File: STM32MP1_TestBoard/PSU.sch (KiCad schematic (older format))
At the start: 19 parts, among them Q1 DMG2302U, U3 SE8233X2, U4 TPS54202DDC, U6 STM32G031JxM, U7 MCP603-xCH

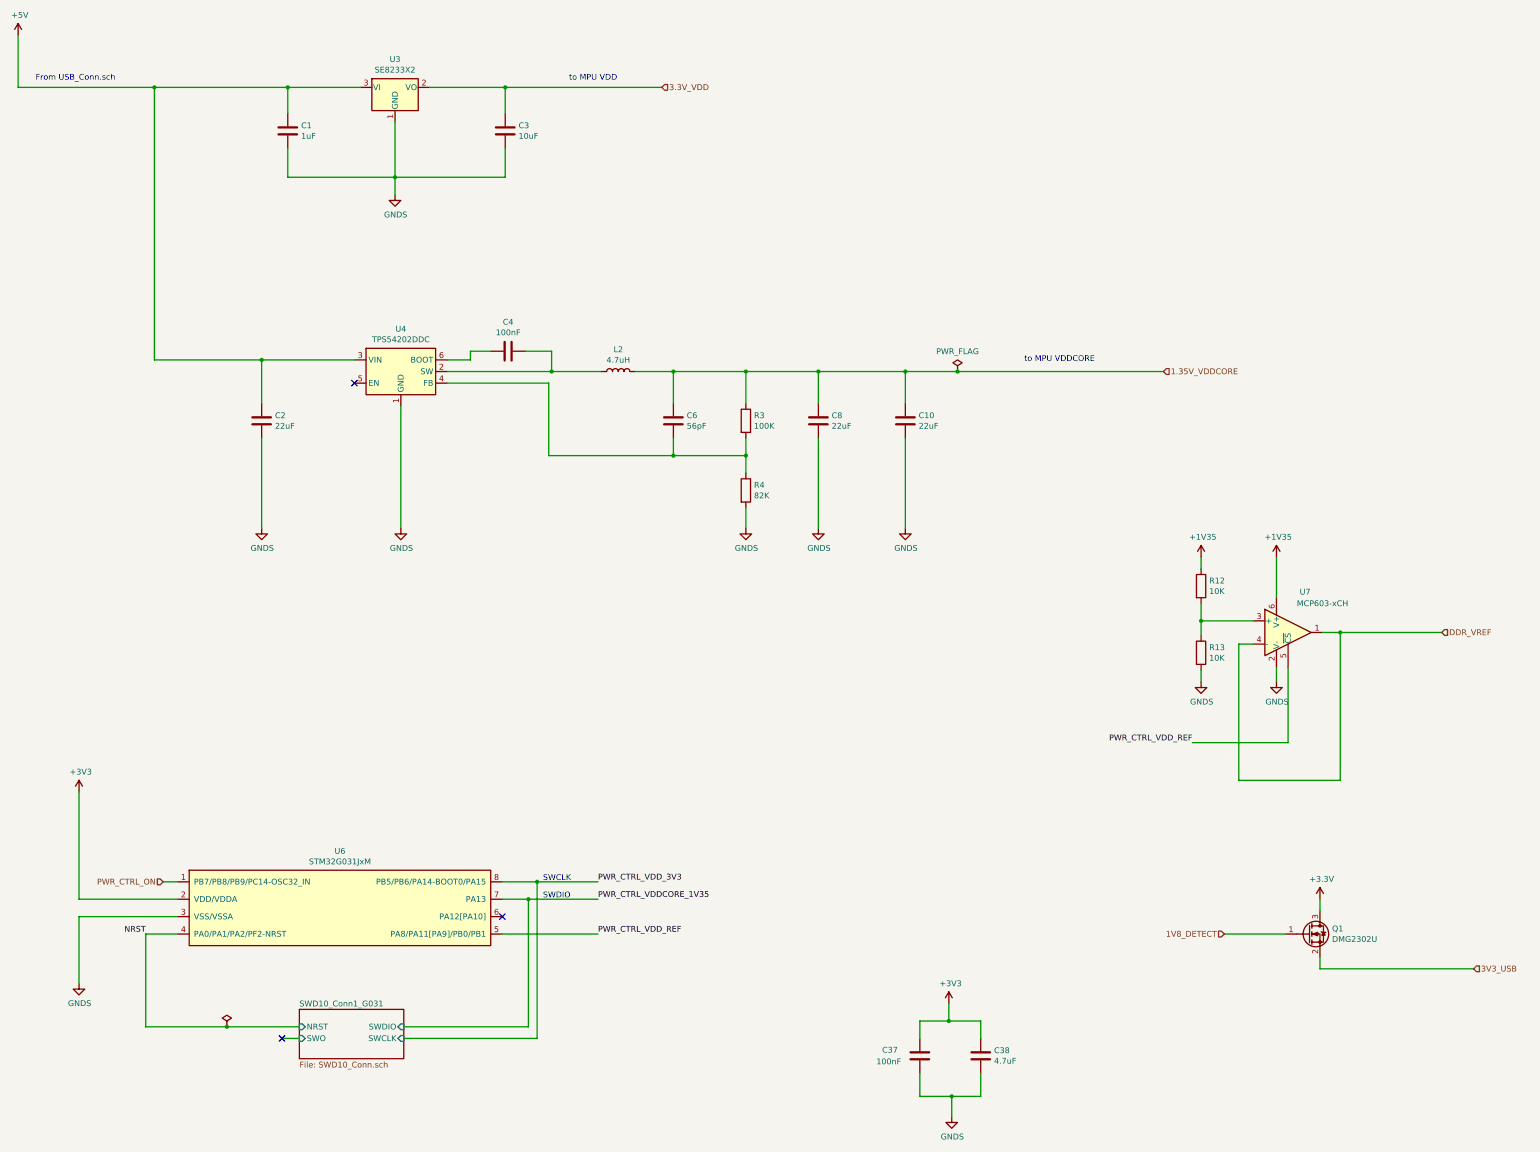
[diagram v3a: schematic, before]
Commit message: updated schematic design
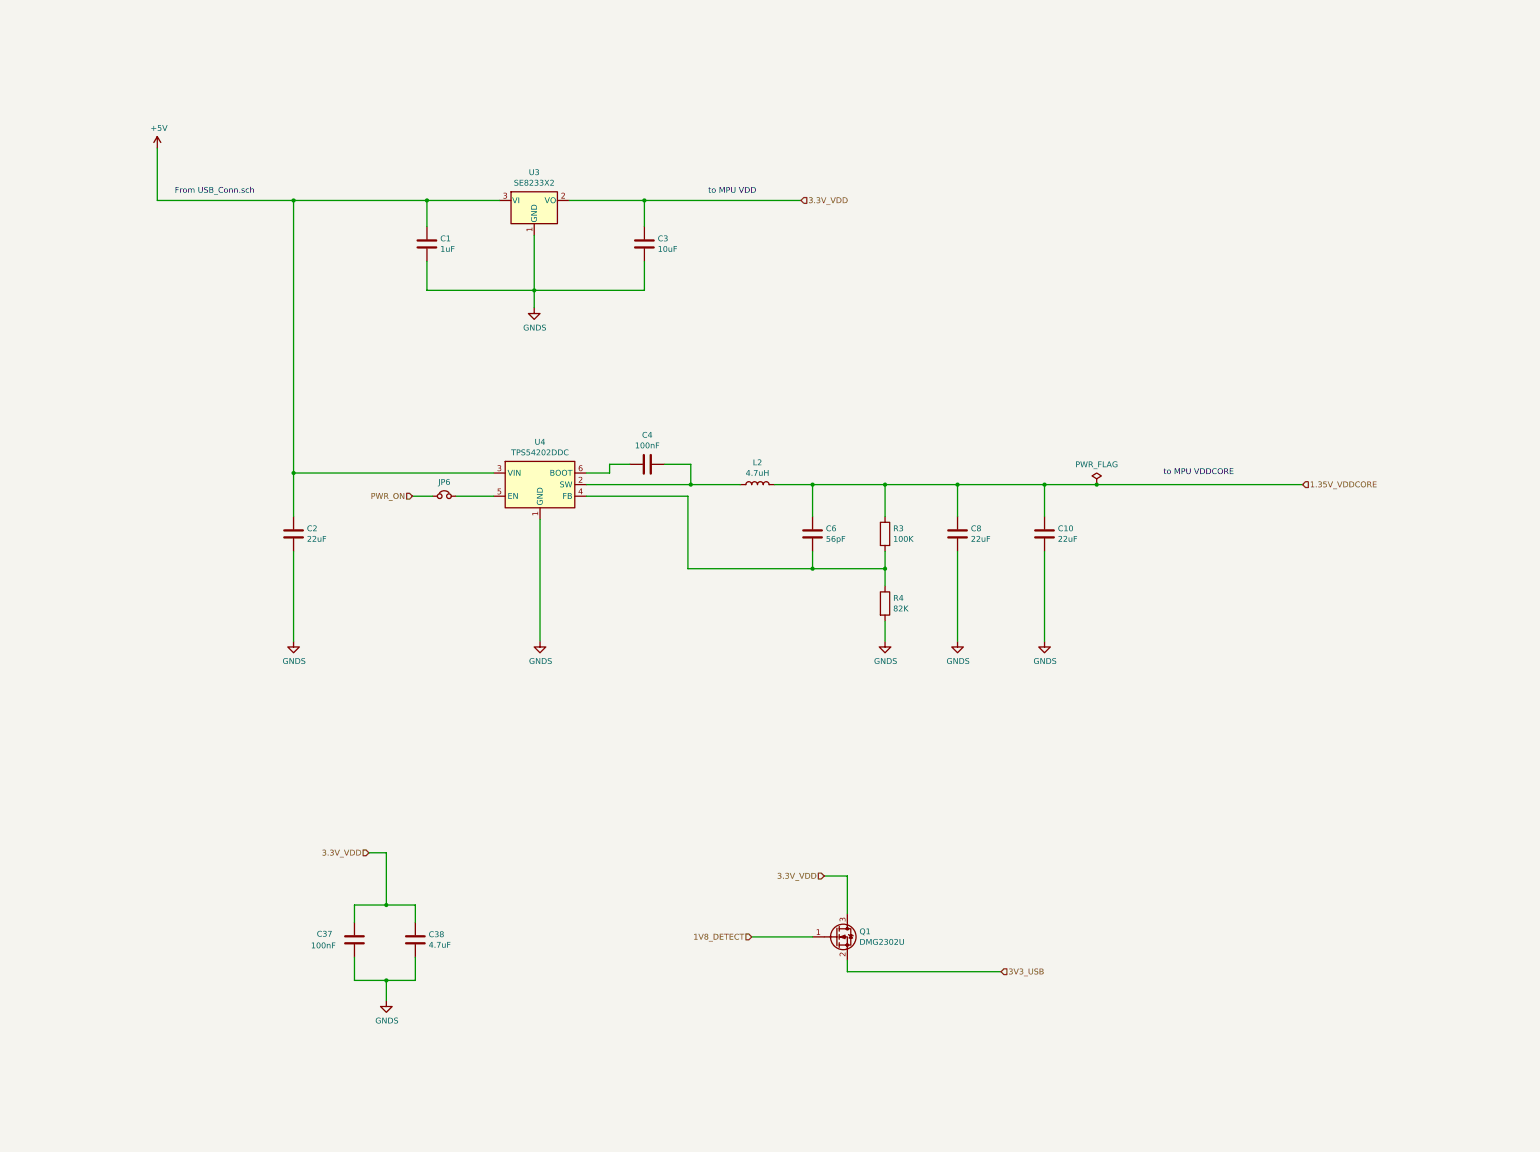
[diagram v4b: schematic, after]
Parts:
- removed R12, R13: 10K, Resistor_SMD:R_0402_1005Metric_Pad0.72x0.64mm_HandSolder, symbol Device:R
- removed U6: STM32G031JxM, Package_SO:SO-8_5.3x6.2mm_P1.27mm, symbol STM32G031:STM32G031JxM
- removed U7: MCP603-xCH, Package_TO_SOT_SMD:SOT-23-6, symbol Amplifier_Operational:MCP603-xCH
- added JP6: Jumper_NC_Small, Jumper:SolderJumper-2_P1.3mm_Bridged_Pad1.0x1.5mm, symbol Device:Jumper_NC_Small
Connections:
- net +3V3 is gone; now on net 3.3V_VDD: C37.1, C38.1, Q1.3 (D)
- net at U4.5 (EN): now also JP6.2
- new net PWR_ON: JP6.1
- no-connect marks 3 -> 0
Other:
- note removed: "SWCLK"
- note removed: "SWDIO"
- moved on the sheet: C1, C10, C2, C3, C37, C38, C4, C6, C8, L2, Q1, R3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

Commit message: layout update
backup. work in progress
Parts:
- removed C37: 100nF, Capacitor_SMD:C_0805_2012Metric_Pad1.18x1.45mm_HandSolder, symbol Device:C
- removed C38: 4.7uF, Capacitor_SMD:C_0805_2012Metric_Pad1.18x1.45mm_HandSolder, symbol Device:C
- added C5: 22uF, Capacitor_SMD:C_1206_3216Metric_Pad1.33x1.80mm_HandSolder, symbol Device:C
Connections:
- net +5V: now also C5.1
- net GNDS: now also C5.2
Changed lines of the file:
@@
 Wire Wire Line
 	4050 5400 4050 5025
-Wire Wire Line
-	4050 5700 4050 6475
 $Comp
 L power:GNDS #PWR03
@@
 Text HLabel 10150 9325 2    50   Input ~ 0
 3V3_USB
-$Comp
-L Device:C C37
-U 1 1 604D0F85
-P 4575 9050
-F 0 "C37" H 4250 9100 50  0000 L CNN
-F 1 "100nF" H 4200 9000 50  0000 L CNN
-F 2 "Capacitor_SMD:C_0805_2012Metric_Pad1.18x1.45mm_HandSolder" H 4613 8900 50  0001 C CNN
-F 3 "~" H 4575 9050 50  0001 C CNN
-F 4 "~" H 4575 9050 50  0001 C CNN "Mfr"
-F 5 "~" H 4575 9050 50  0001 C CNN "PartNo"
-	1    4575 9050
-	1    0    0    -1
-$EndComp
-$Comp
-L Device:C C38
-U 1 1 604D14DF
-P 5100 9050
-F 0 "C38" H 5215 9096 50  0000 L CNN
-F 1 "4.7uF" H 5215 9005 50  0000 L CNN
-F 2 "Capacitor_SMD:C_0805_2012Metric_Pad1.18x1.45mm_HandSolder" H 5138 8900 50  0001 C CNN
-F 3 "~" H 5100 9050 50  0001 C CNN
-F 4 "~" H 5100 9050 50  0001 C CNN "Mfr"
-F 5 "~" H 5100 9050 50  0001 C CNN "PartNo"
-	1    5100 9050
-	1    0    0    -1
-$EndComp
-Wire Wire Line
-	5100 8900 5100 8750
-Wire Wire Line
-	4575 8750 4575 8900
-Wire Wire Line
-	4575 9200 4575 9400
-Wire Wire Line
-	4575 9400 4850 9400
-Wire Wire Line
-	5100 9400 5100 9200
-Wire Wire Line
-	4850 9400 4850 9575
-Connection ~ 4850 9400
-Wire Wire Line
-	4850 9400 5100 9400
-$Comp
-L power:GNDS #PWR042
-U 1 1 604DD164
-P 4850 9575
-F 0 "#PWR042" H 4850 9325 50  0001 C CNN
-F 1 "GNDS" H 4855 9402 50  0000 C CNN
-F 2 "" H 4850 9575 50  0001 C CNN
-F 3 "" H 4850 9575 50  0001 C CNN
-	1    4850 9575
-	1    0    0    -1
-$EndComp
 Wire Wire Line
 	8525 9025 8000 9025
@@
 PWR_ON
 Wire Wire Line
-	4050 5025 5775 5025
+	4050 5025 4500 5025
 Connection ~ 4050 5025
 $Comp
@@
 Wire Wire Line
 	8825 8500 8825 8825
-Wire Wire Line
-	4850 8750 4850 8300
-Text HLabel 4700 8300 0    50   Input ~ 0
-3.3V_VDD
-Wire Wire Line
-	4700 8300 4850 8300
-Wire Wire Line
-	4575 8750 4850 8750
-Connection ~ 4850 8750
-Wire Wire Line
-	4850 8750 5100 8750
+$Comp
+L Device:C C5
+U 1 1 5FC7AF91
+P 4500 5550
+F 0 "C5" H 4615 5596 50  0000 L CNN
+F 1 "22uF" H 4615 5505 50  0000 L CNN
+F 2 "Capacitor_SMD:C_1206_3216Metric_Pad1.33x1.80mm_HandSolder" H 4538 5400 50  0001 C CNN
+F 3 "https://www.mouser.co.uk/datasheet/2/212/KEM_C1006_X5R_SMD-1103249.pdf" H 4500 5550 50  0001 C CNN
+F 4 "C1206C226M8PACTU" H 4500 5550 50  0001 C CNN "PartNo"
+F 5 "Kemet" H 4500 5550 50  0001 C CNN "Mfr"
+	1    4500 5550
+	1    0    0    -1
+$EndComp
+Wire Wire Line
+	4500 5400 4500 5025
+Wire Wire Line
+	4500 5700 4500 5975
+Wire Wire Line
+	4500 5975 4050 5975
+Wire Wire Line
+	4050 5700 4050 5975
+Connection ~ 4050 5975
+Wire Wire Line
+	4050 5975 4050 6475
+Connection ~ 4500 5025
+Wire Wire Line
+	4500 5025 5775 5025
 $EndSCHEMATC

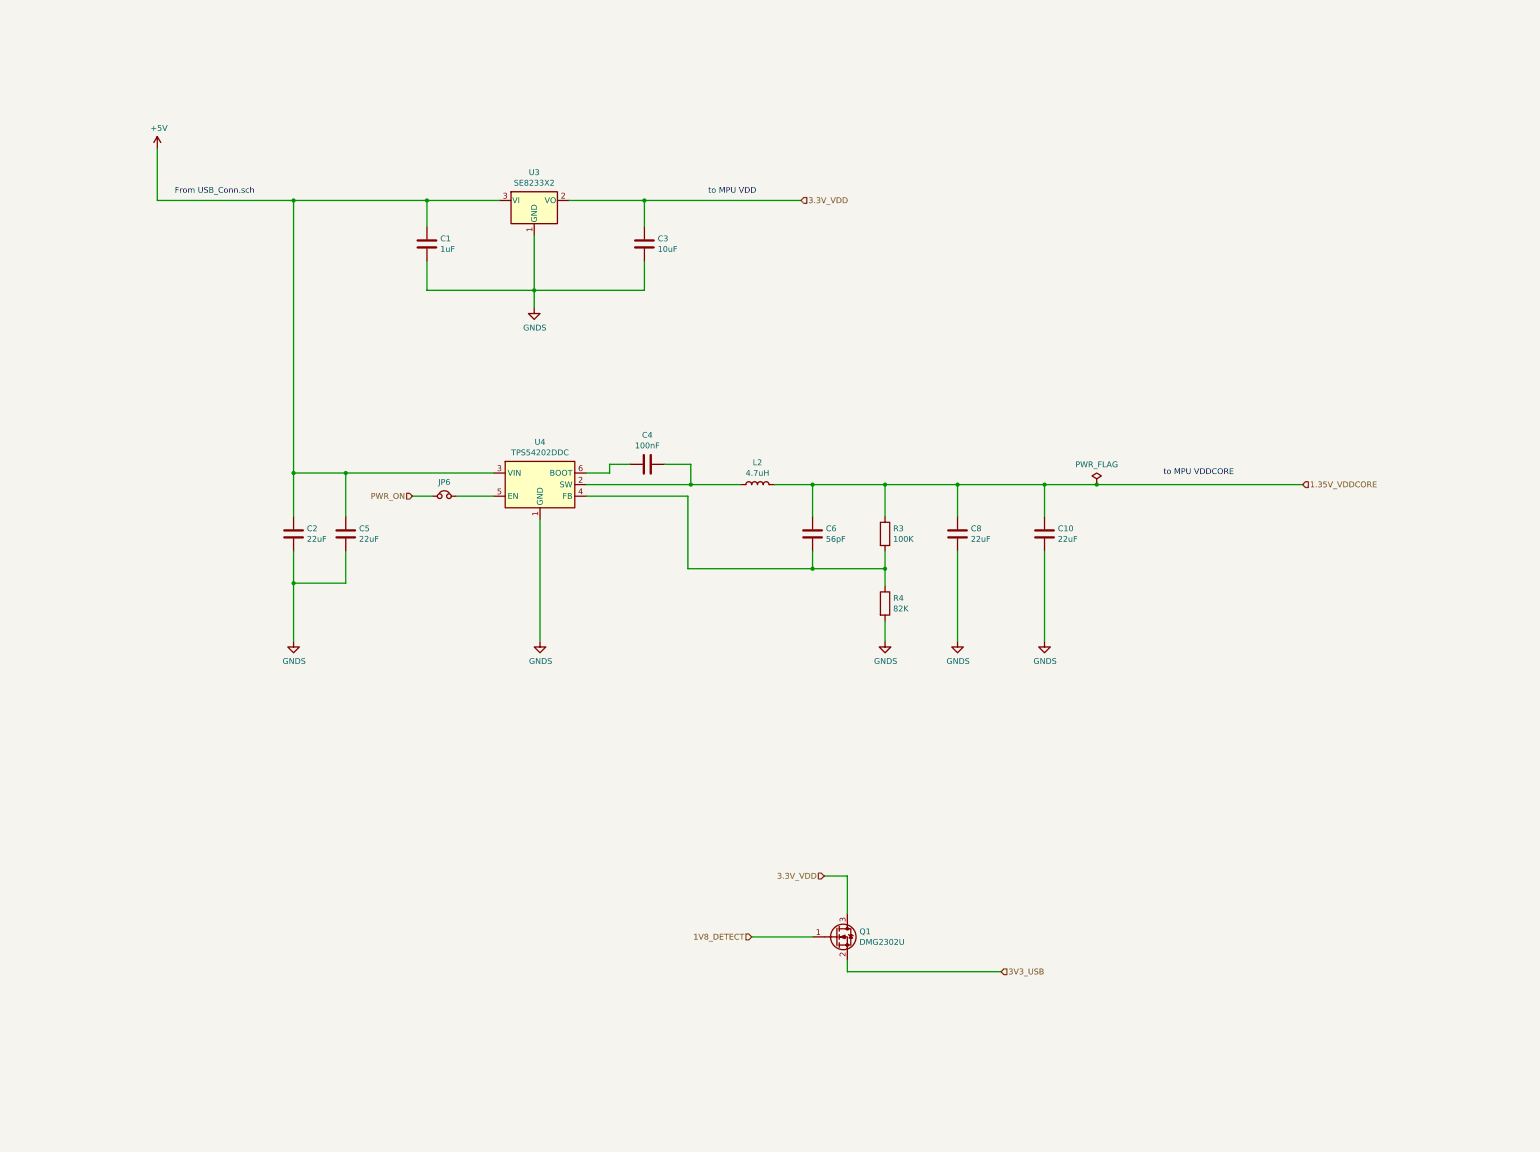
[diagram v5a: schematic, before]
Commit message: added psu
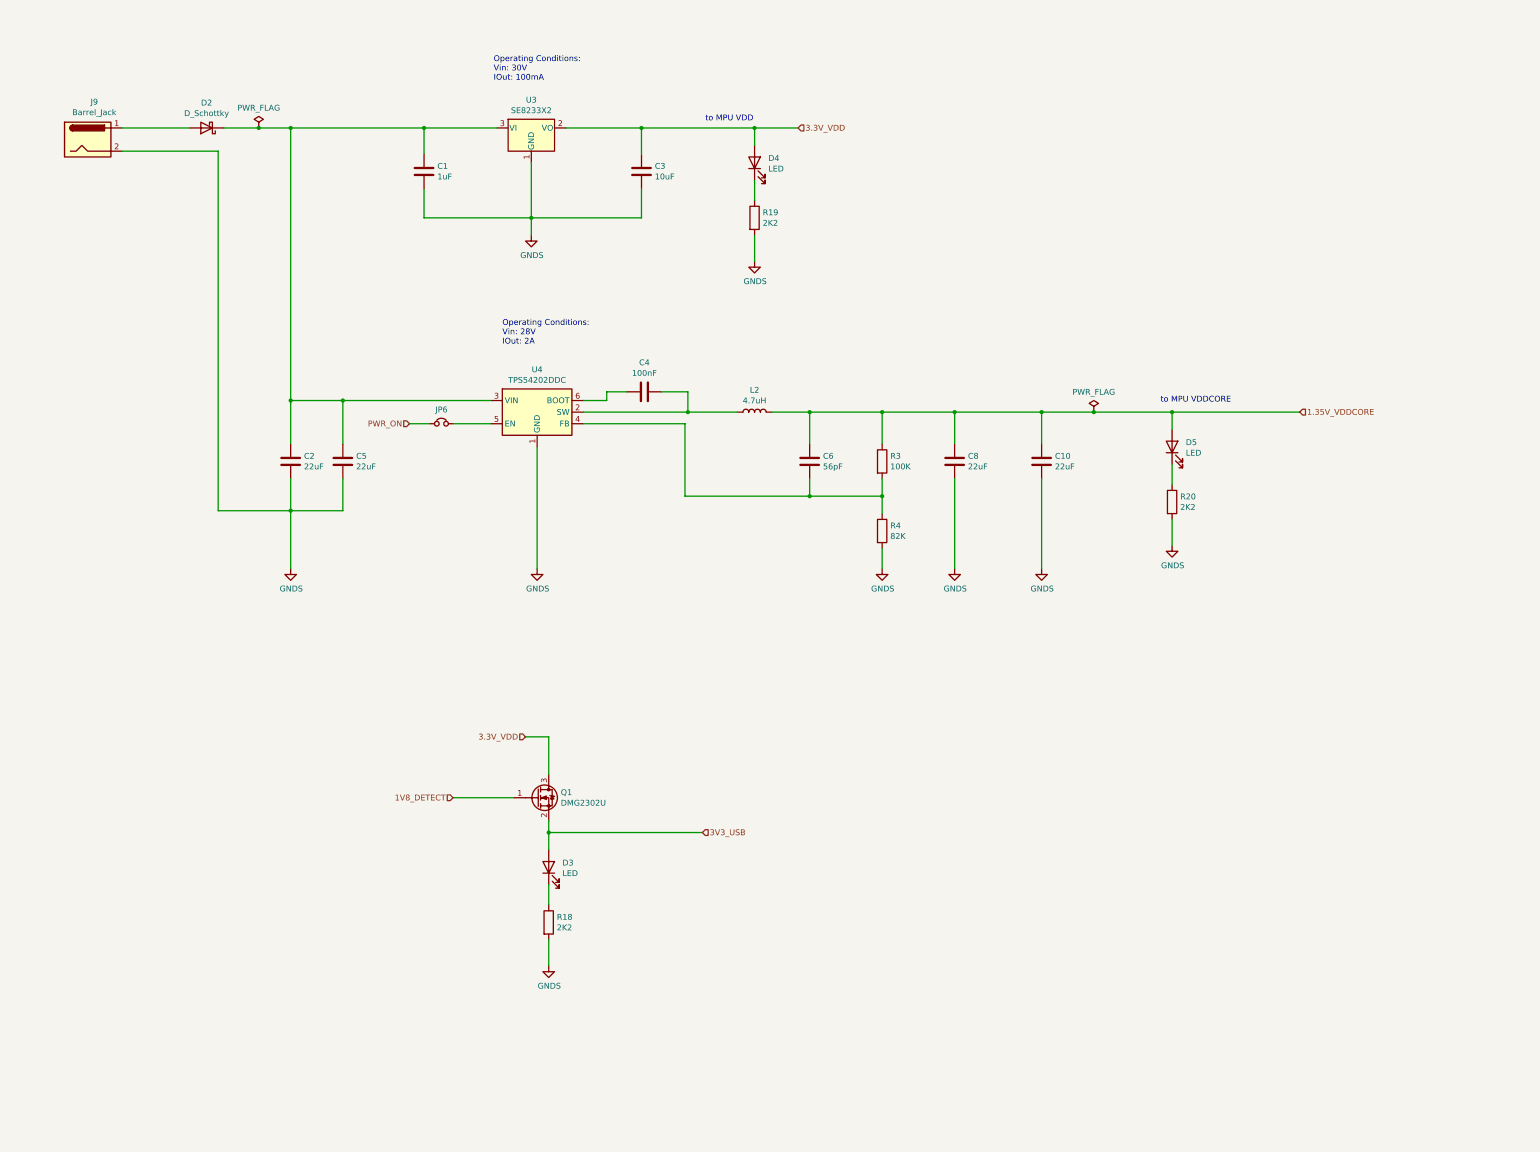
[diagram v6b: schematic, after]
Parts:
- added D2: D_Schottky, Diode_SMD:D_SOD-123F, symbol Device:D_Schottky
- added D3, D4, D5: LED, LED_SMD:LED_0805_2012Metric_Pad1.15x1.40mm_HandSolder, symbol Device:LED
- added J9: Barrel_Jack, Connector_BarrelJack:BarrelJack_Horizontal, symbol Connector:Barrel_Jack
- added R18, R19, R20: 2K2, Resistor_SMD:R_0402_1005Metric_Pad0.72x0.64mm_HandSolder, symbol Device:R
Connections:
- net 1.35V_VDDCORE: now also D5.2 (A)
- net 3.3V_VDD: now also D4.2 (A)
- net 3V3_USB: now also D3.2 (A)
- net GNDS: now also J9.2, R18.2, R19.2, R20.2
- net +5V: no longer names the net of C1.1, C2.1, C5.1, U3.3 (VI), U4.3 (VIN)
- net +5V: now also D2.1 (K)
- new net: D2.2 (A), J9.1
- new net: D4.1 (K), R19.1
- new net: D5.1 (K), R20.1
- new net: D3.1 (K), R18.1
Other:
- note added: "Operating Conditions: \nVin: 30V\nIOut: 100mA"
- note added: "Operating Conditions:\nVin: 28V\nIOut: 2A"
- note removed: "From USB_Conn.sch"
- moved on the sheet: C1, C10, C2, C3, C4, C5, C6, C8, JP6, L2, Q1, R3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

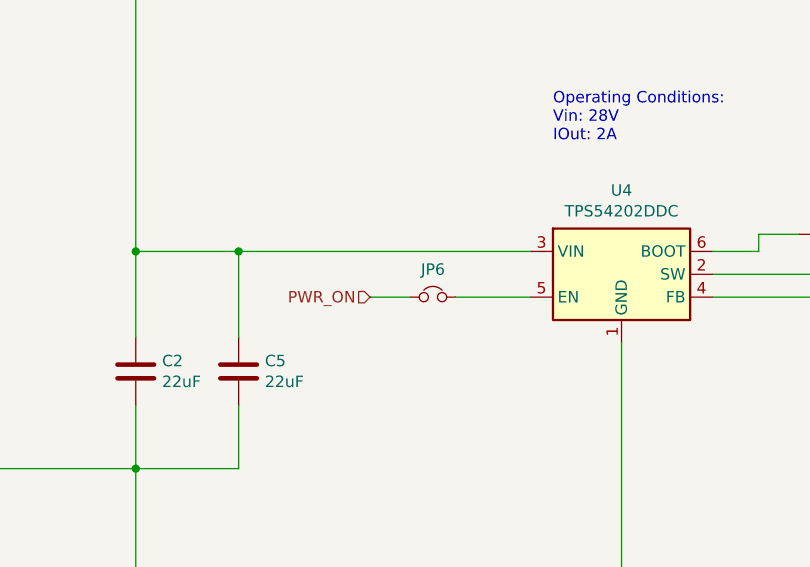
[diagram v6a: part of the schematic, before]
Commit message: swapped DDR3 high/low strobe diff pairs
- corrected DRC errors
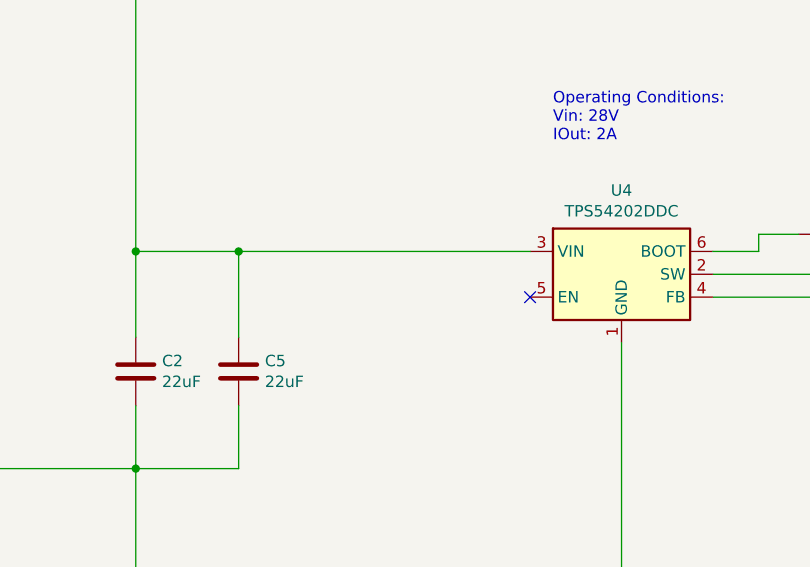
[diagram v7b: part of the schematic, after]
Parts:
- removed JP6: Jumper_NC_Small, Jumper:SolderJumper-2_P1.3mm_Bridged_Pad1.0x1.5mm, symbol Device:Jumper_NC_Small
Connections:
- no-connect marks 0 -> 1
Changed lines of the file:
@@
 1V8_DETECT
-Wire Wire Line
-	5750 4600 5425 4600
-Text HLabel 5050 4600 0    50   Input ~ 0
-PWR_ON
 Wire Wire Line
 	4025 4400 4475 4400
 Connection ~ 4025 4400
-$Comp
-L Device:Jumper_NC_Small JP6
-U 1 1 6090B4C9
-P 5325 4600
-F 0 "JP6" H 5325 4721 50  0000 C CNN
-F 1 "Jumper_NC_Small" H 5325 4721 50  0001 C CNN
-F 2 "Jumper:SolderJumper-2_P1.3mm_Bridged_Pad1.0x1.5mm" H 5325 4600 50  0001 C CNN
-F 3 "~" H 5325 4600 50  0001 C CNN
-	1    5325 4600
-	1    0    0    -1
-$EndComp
-Wire Wire Line
-	5225 4600 5050 4600
 Text HLabel 6050 7300 0    50   Input ~ 0
 3.3V_VDD
@@
 $EndComp
 Connection ~ 6250 8125
+NoConn ~ 5750 4600
 $EndSCHEMATC
